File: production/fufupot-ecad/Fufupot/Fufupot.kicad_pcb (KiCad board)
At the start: 4 copper layers, 127 x 127 mm, 56 parts, among them IC1 FOD3150, J1 Conn_01x04, J10 Conn_01x03, J11 Conn_01x03, J12 Conn_01x02, J2 USB_B, J3 Conn_01x03, J4 Conn_01x02, J5 Conn_01x02, J6 Conn_01x02, J7 Conn_01x02, J8 Conn_01x04, J9 Conn_01x02, SW1 SW_Push, SW2 SW_Push, U1 USBLC6-2SC6, U2 LM5165DRC, U3 FT232RL, U4 ATMEGA328P-PN, U5 STGP8NC60KD

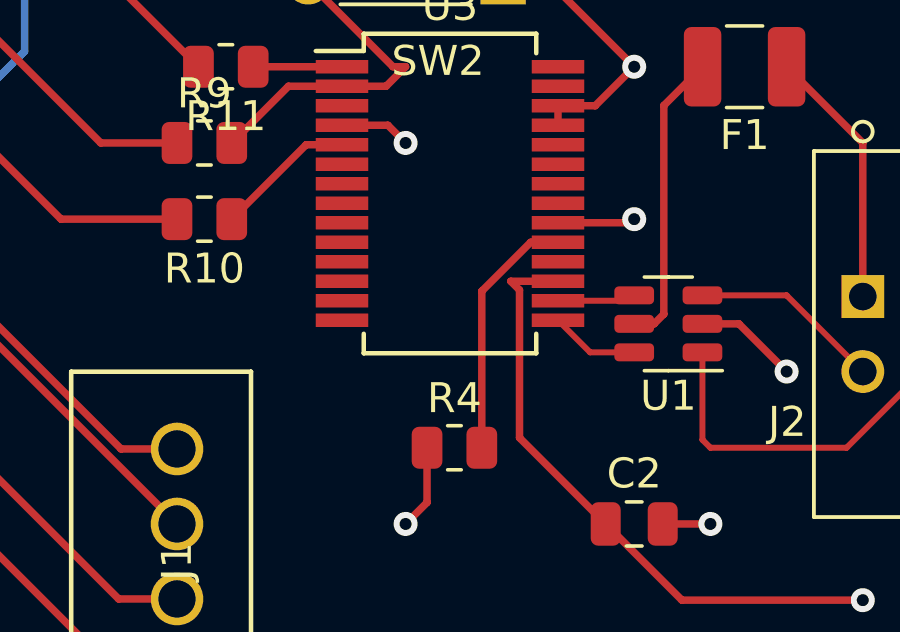
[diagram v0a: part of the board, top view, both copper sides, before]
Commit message: fixed gnd of usb on pcb
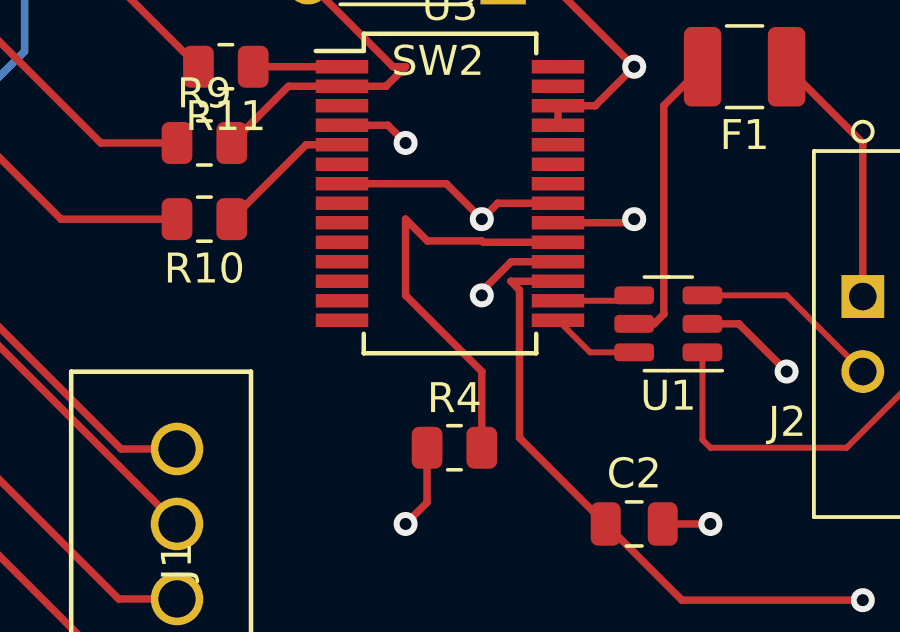
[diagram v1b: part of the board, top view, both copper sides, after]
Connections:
- U3 pad 18: unconnected-(U3-GND-Pad18) -> GND
- U3 pad 21: unconnected-(U3-GND-Pad21) -> GND
- U3 pad 7: unconnected-(U3-GND-Pad7) -> GND
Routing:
- net GND: track 138.7 -> 149.7 mm, vias 22 -> 24
- net Net-(U3-~{RESET}): track 8.43 -> 14.1 mm

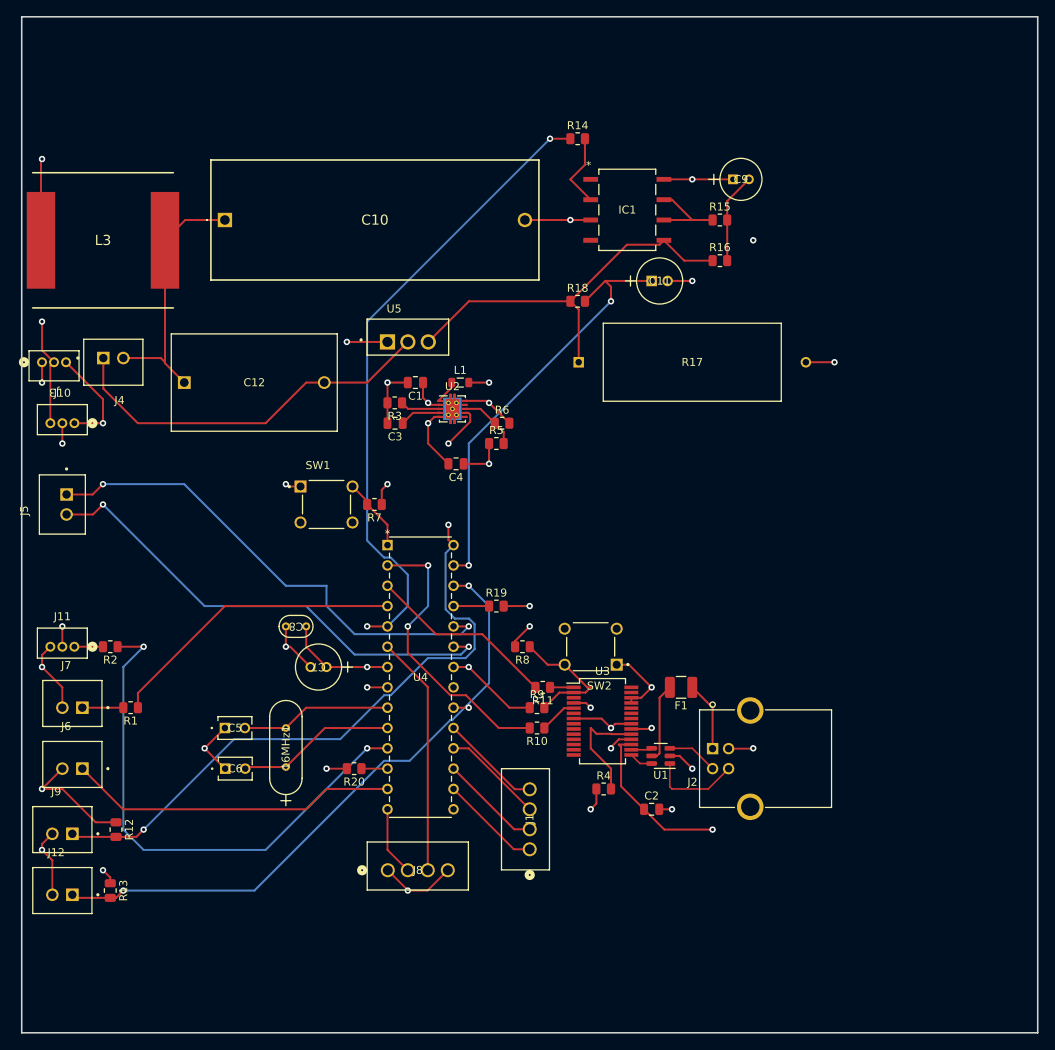
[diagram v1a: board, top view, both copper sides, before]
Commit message: make pcb more compact
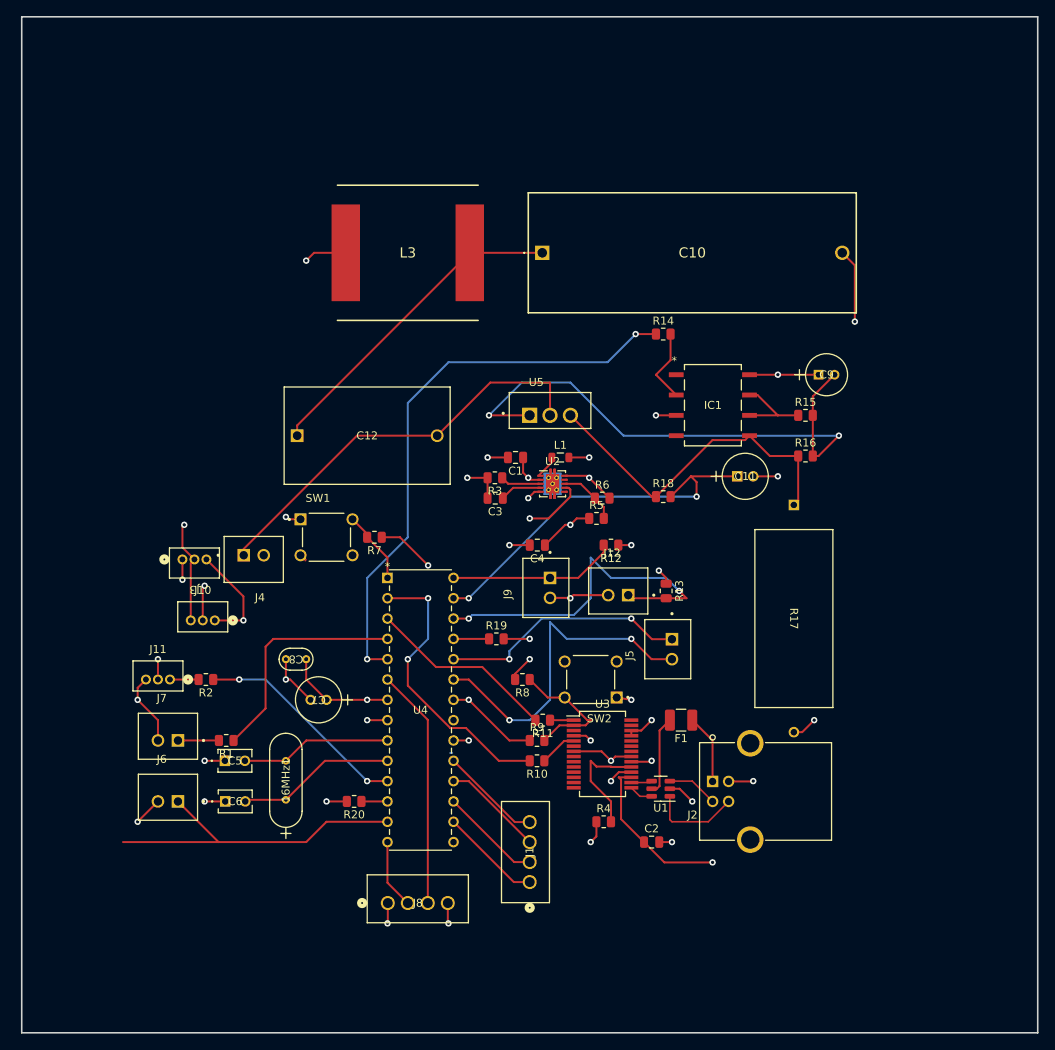
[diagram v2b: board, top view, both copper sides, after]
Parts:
- moved R13 78.9 mm to (126.3, 109.9)
- moved J12 78.9 mm to (120.3, 109.9)
- moved J5 77.8 mm to (126.5, 117.1)
- moved R12 71.4 mm to (119.4, 104.1), turned to 180 degrees
- moved J9 67.6 mm to (111.2, 109.5), turned to 90 degrees
- moved C10 39.9 mm to (110.8, 67.6)
- moved L3 38.1 mm to (94.0, 67.6)
- moved R17 32.3 mm to (142.2, 99.1), turned to -90 degrees
- moved J3 30.3 mm to (65.8, 105.9)
- moved J4 30.3 mm to (74.7, 105.9)
- moved J10 30.3 mm to (69.8, 113.5)
- moved IC1 26.7 mm to (132.1, 86.6)
- moved C11 26.7 mm to (135.2, 95.5)
- moved C9 26.7 mm to (145.3, 82.8)
- moved R14 26.7 mm to (125.9, 77.8)
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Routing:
- net A2: track 78.9 -> 21.0 mm, vias 2 -> 0
- net Net-(IC1-VSS): track 66.3 -> 112.1 mm
- net D_LEDStrip: track 66.5 -> 27.0 mm
- net A3: track 78.5 -> 45.0 mm
- net A5: track 62.4 -> 31.1 mm
- net GND: track 149.7 -> 129.6 mm, vias 24 -> 31
- net A4: track 60.9 -> 42.1 mm
- net Net-(J4-Pin_2): track 32.7 -> 41.7 mm
- net D_LED: track 37.5 -> 29.0 mm
- net D9: track 79.1 -> 71.3 mm
- net A1: track 54.5 -> 47.9 mm
- net VCC: track 6.13 -> 10.5 mm
- net Net-(J4-Pin_1): track 47.9 -> 51.8 mm
- net +48V: track 33.5 -> 30.3 mm
- net +16V: track 8.26 -> 9.46 mm
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
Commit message: Changed pcb mounts
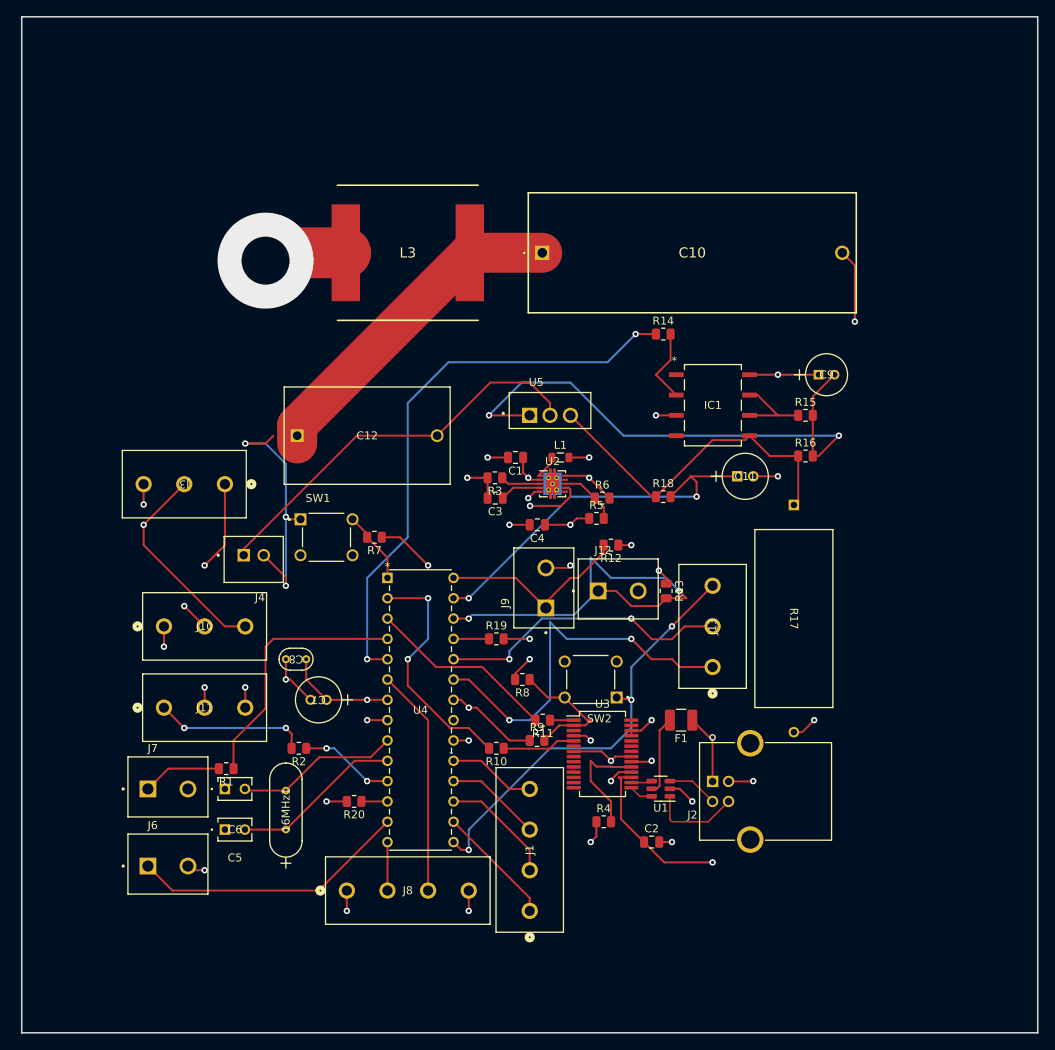
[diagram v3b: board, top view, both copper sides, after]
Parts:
- removed J5: Conn_01x02, B2B-XH-A_LF__SN_:JST_B2B-XH-A_LF__SN_
- added J13: Conn_01x03, pcbmount3footprints:282837-3_TYC, F.Cu at (132.1, 119.4)
- J1, J8: footprint 4PINfootprints:CONN_B4B-XH-A_JST -> pcbmount4footprints:282837-4_TYC
- J10, J11, J3: footprint 3PINfootprints:CONN_B3B-ZR_JST -> pcbmount3footprints:282837-3_TYC
- J12, J6, J7, J9: footprint B2B-XH-A_LF__SN_:JST_B2B-XH-A_LF__SN_ -> KF301-2P:HANDSON_KF301-2P
- moved R2 14.5 mm to (80.4, 129.5)
- moved J3 10.8 mm to (71.1, 96.5)
- moved J6 8.60 mm to (64.0, 144.3)
- moved J7 6.59 mm to (64.0, 134.6)
- moved J10 6.39 mm to (63.5, 114.3)
- moved J8 5.35 mm to (86.4, 147.3)
- moved R10 5.31 mm to (105.1, 129.5)
- moved 16MHz1 3.72 mm to (78.7, 139.7)
- moved J1 3.60 mm to (109.2, 149.9)
- moved J11 3.60 mm to (63.5, 124.5)
- moved C6 3.52 mm to (71.1, 139.7)
- moved C5 3.52 mm to (71.1, 134.6)
- moved R1 3.52 mm to (71.3, 132.1)
- moved C4 2.54 mm to (110.2, 101.6)
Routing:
- net PWM Speed Control: track 0.00 -> 52.4 mm, vias 0 -> 2
- net Net-(J4-Pin_2): track 41.7 -> 73.1 mm, vias 0 -> 2
- net GND: track 129.6 -> 108.5 mm, vias 31 -> 30
- net +48V: track 30.3 -> 48.5 mm
- net Net-(J11-Pin_1): track 3.58 -> 19.1 mm, vias 0 -> 2
- net D_LEDStrip: track 27.0 -> 11.9 mm
- net D_Buzz: track 41.3 -> 34.8 mm
- net A5: track 31.1 -> 36.8 mm
- net RX: track 36.2 -> 30.5 mm
- net A4: track 42.1 -> 47.6 mm
- net Net-(J7-Pin_1): track 5.12 -> 9.92 mm
- net A3: track 45.0 -> 49.8 mm
- net Net-(U3-RXD): track 4.70 -> 9.17 mm
- net +5V: track 40.4 -> 44.0 mm
- net D_LED: track 29.0 -> 32.5 mm
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
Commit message: Final Draft, Need to be checked by Andy
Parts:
- moved J4 25.7 mm to (91.4, 86.4), turned to 0 degrees
- moved L3 23.8 mm to (71.1, 61.1), turned to -90 degrees
- moved C10 23.5 mm to (90.5, 55.9)
- moved C12 17.6 mm to (85.2, 73.7)
- moved R17 10.5 mm to (152.4, 101.6)
- moved J13 7.62 mm to (139.7, 119.4)
- moved L1 5.32 mm to (118.3, 94.0)
- moved R11 1.72 mm to (110.1, 124.5)
- moved R13 0.72 mm to (127.0, 109.9)
- turned U5 to -90 degrees
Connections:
- C9 pad 1: +15V -> +16V
- IC1 pad 8: +15V -> +16V
- R7 pad 1: VCC -> +5V
- R8 pad 2: VCC -> +5V
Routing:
- net RX: track 30.5 -> 71.2 mm, vias 2 -> 4
- net +5V: track 44.0 -> 66.2 mm, vias 9 -> 10
- net Net-(J4-Pin_2): track 73.1 -> 51.3 mm, vias 2 -> 0
- net GND: track 108.5 -> 90.5 mm, vias 30 -> 33
- net TX: track 23.8 -> 41.2 mm, vias 0 -> 2
- net Net-(J4-Pin_1): track 50.3 -> 33.3 mm
- net VCC: track 10.5 -> 0.00 mm, vias 2 -> 0
- net +48V: track 48.5 -> 38.1 mm, vias 4 -> 6
- net +16V: track 8.40 -> 18.1 mm, vias 2 -> 3
- net +15V: track 8.62 -> 0.00 mm, vias 1 -> 0
- net PWM Speed Control: track 52.4 -> 60.0 mm
- net A5: track 36.8 -> 44.4 mm
- net Net-(IC1-VSS): track 112.1 -> 116.8 mm
- net Net-(U2-SW): track 2.98 -> 7.56 mm
- net A4: track 47.6 -> 51.7 mm
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- added copper zone on F.Cu, net (none)
- added copper zone on F.Cu, net +48V
- added copper zone on F.Cu, net GND

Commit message: Actual Final Draft- No errors
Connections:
- R15 pad 2: Net-(IC1-VSS) -> Net-(U5-G)
- R16 pad 1: Net-(IC1-VSS) -> Net-(U5-G)
- U5 pad 1: Net-(IC1-VSS) -> Net-(U5-G)
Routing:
- net Net-(U5-G): track 0.00 -> 42.3 mm, vias 0 -> 2
- net Net-(IC1-VSS): track 116.8 -> 103.1 mm
